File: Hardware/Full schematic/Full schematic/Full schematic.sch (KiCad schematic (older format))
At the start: 170 parts, among them J1 Conn_01x04_Male, J2 Conn_01x03_Male, J3 Conn_01x02_Male, J4 Conn_01x04_Male, J5 Conn_01x03_Male, J6 Conn_01x02_Male, J7 Conn_01x02_Male, J8 Conn_01x02_Male, J9 Conn_01x07_Male, K1 EDR101A0500, K2 EDR101A0500, K3 EDR101A0500, K4 EDR101A0500, K5 EDR101A0500, K6 EDR101A0500, Q1 BC847, Q10 IRLML2502, Q11 IRLML2502, Q12 IRLML2502, Q13 IRLML2502, Q2 BSS138, Q3 BC847, Q4 IRF610, Q5 BSS138, Q6 BFS17, Q7 AFT05MS003N, Q8 IRLML2502, Q9 IRLML2502, U1 74LVC2T45DC, U2 74LVC2T45DC, U3 AD9835, U4 ICS501, X1 50MHz

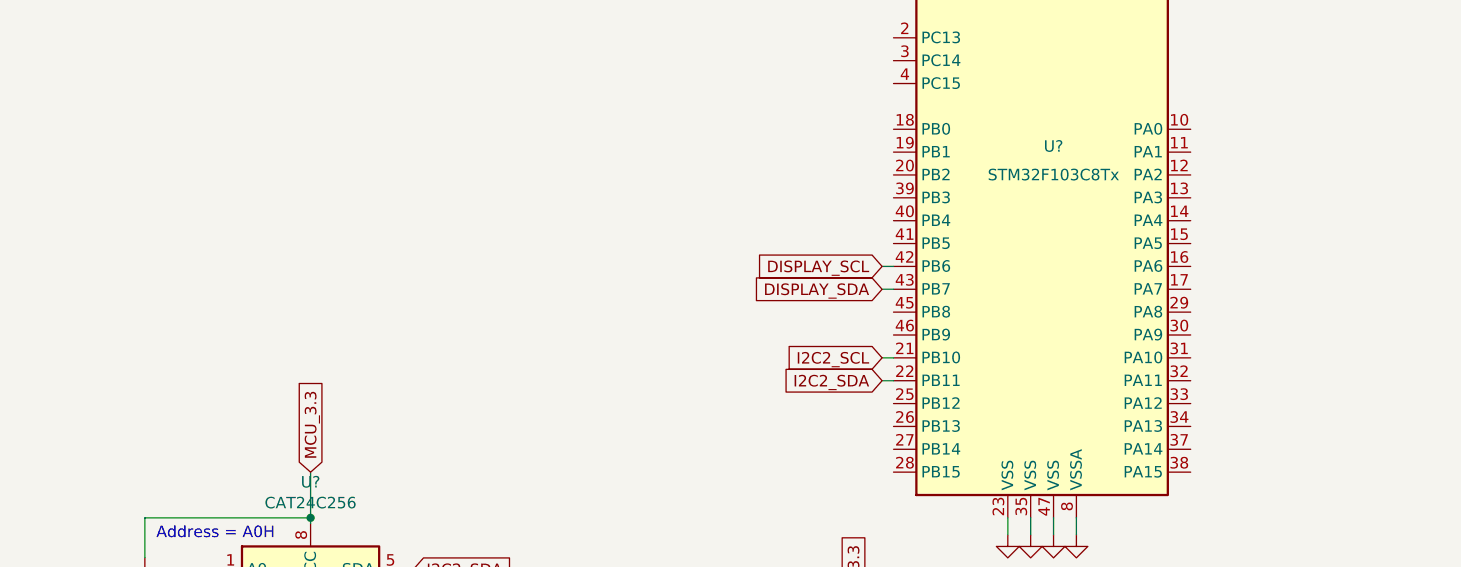
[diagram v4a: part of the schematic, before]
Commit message: Able to get packets via bluetooth
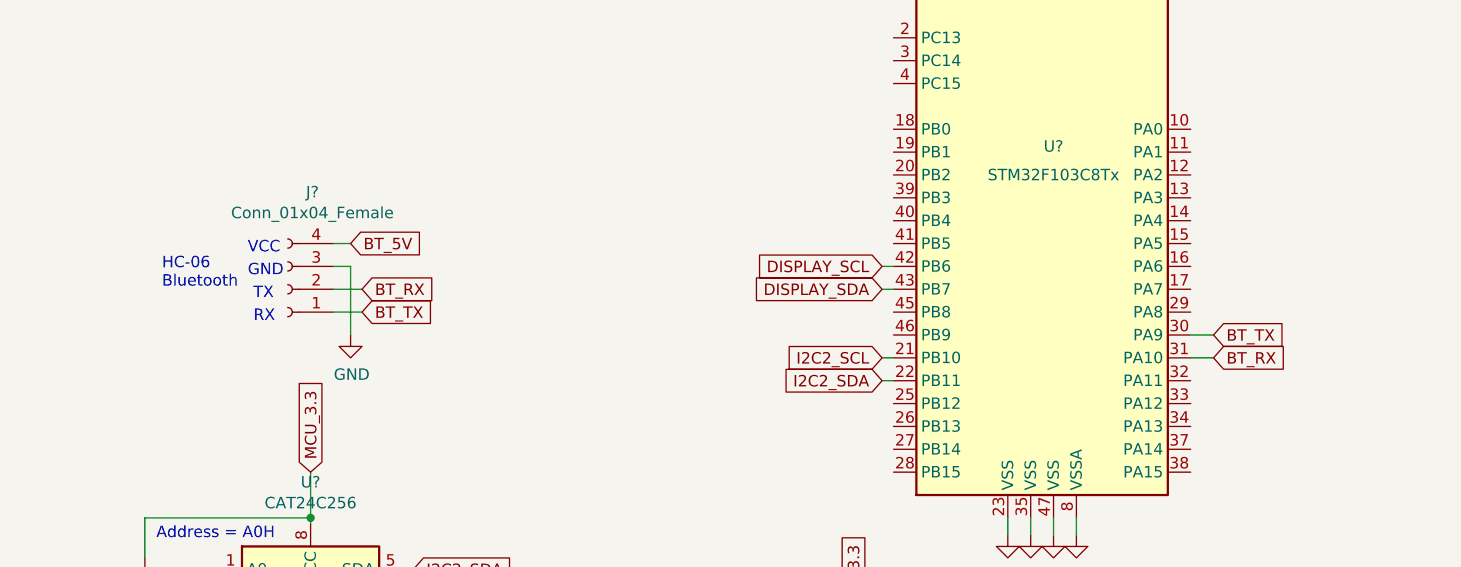
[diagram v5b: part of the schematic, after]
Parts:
- added J?: Conn_01x04_Female, symbol Connector:Conn_01x04_Female
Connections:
- net GND: now also J?.3 (Pin_3)
- net BT_TX: now reaches U?.30 (PA9)
- net BT_TX: now also J?.1 (Pin_1)
- net BT_RX: now reaches U?.31 (PA10)
- net BT_RX: now also J?.2 (Pin_2)
- new net BT_5V: J?.4 (Pin_4)
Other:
- note added: "HC-06\nBluetooth"
- note added: "RX"
- note added: "TX"
- note added: "VCC"
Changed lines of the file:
@@
 Text Notes 5725 16075 0    50   ~ 0
 Address = A0H
+$Comp
+L Connector:Conn_01x04_Female J?
+U 1 1 608B1D74
+P 6300 14975
+F 0 "J?" H 6192 14550 50  0000 C CNN
+F 1 "Conn_01x04_Female" H 6192 14641 50  0000 C CNN
+F 2 "" H 6300 14975 50  0001 C CNN
+F 3 "~" H 6300 14975 50  0001 C CNN
+	1    6300 14975
+	-1   0    0    1
+$EndComp
+Text Notes 6150 15125 0    50   ~ 0
+RX
+Text Notes 6150 15025 0    50   ~ 0
+TX
+Text Notes 6125 14925 0    50   ~ 0
+GND
+Text Notes 6125 14825 0    50   ~ 0
+VCC
+Text Notes 5750 14975 0    50   ~ 0
+HC-06\nBluetooth
+$Comp
+L power:GND #PWR?
+U 1 1 6097477B
+P 6575 15175
+F 0 "#PWR?" H 6575 14925 50  0001 C CNN
+F 1 "GND" H 6580 15002 50  0000 C CNN
+F 2 "" H 6575 15175 50  0001 C CNN
+F 3 "" H 6575 15175 50  0001 C CNN
+	1    6575 15175
+	1    0    0    -1
+$EndComp
+Wire Wire Line
+	6575 15175 6575 14875
+Wire Wire Line
+	6575 14875 6500 14875
+Text GLabel 6575 14775 2    50   Input ~ 0
+BT_5V
+Wire Wire Line
+	6575 14775 6500 14775
+Text GLabel 10350 15175 2    50   Input ~ 0
+BT_TX
+Text GLabel 10350 15275 2    50   Input ~ 0
+BT_RX
+Wire Wire Line
+	10350 15175 10250 15175
+Wire Wire Line
+	10350 15275 10250 15275
+Text GLabel 6625 15075 2    50   Input ~ 0
+BT_TX
+Text GLabel 6625 14975 2    50   Input ~ 0
+BT_RX
+Wire Wire Line
+	6500 14975 6625 14975
+Wire Wire Line
+	6500 15075 6625 15075
 $EndSCHEMATC

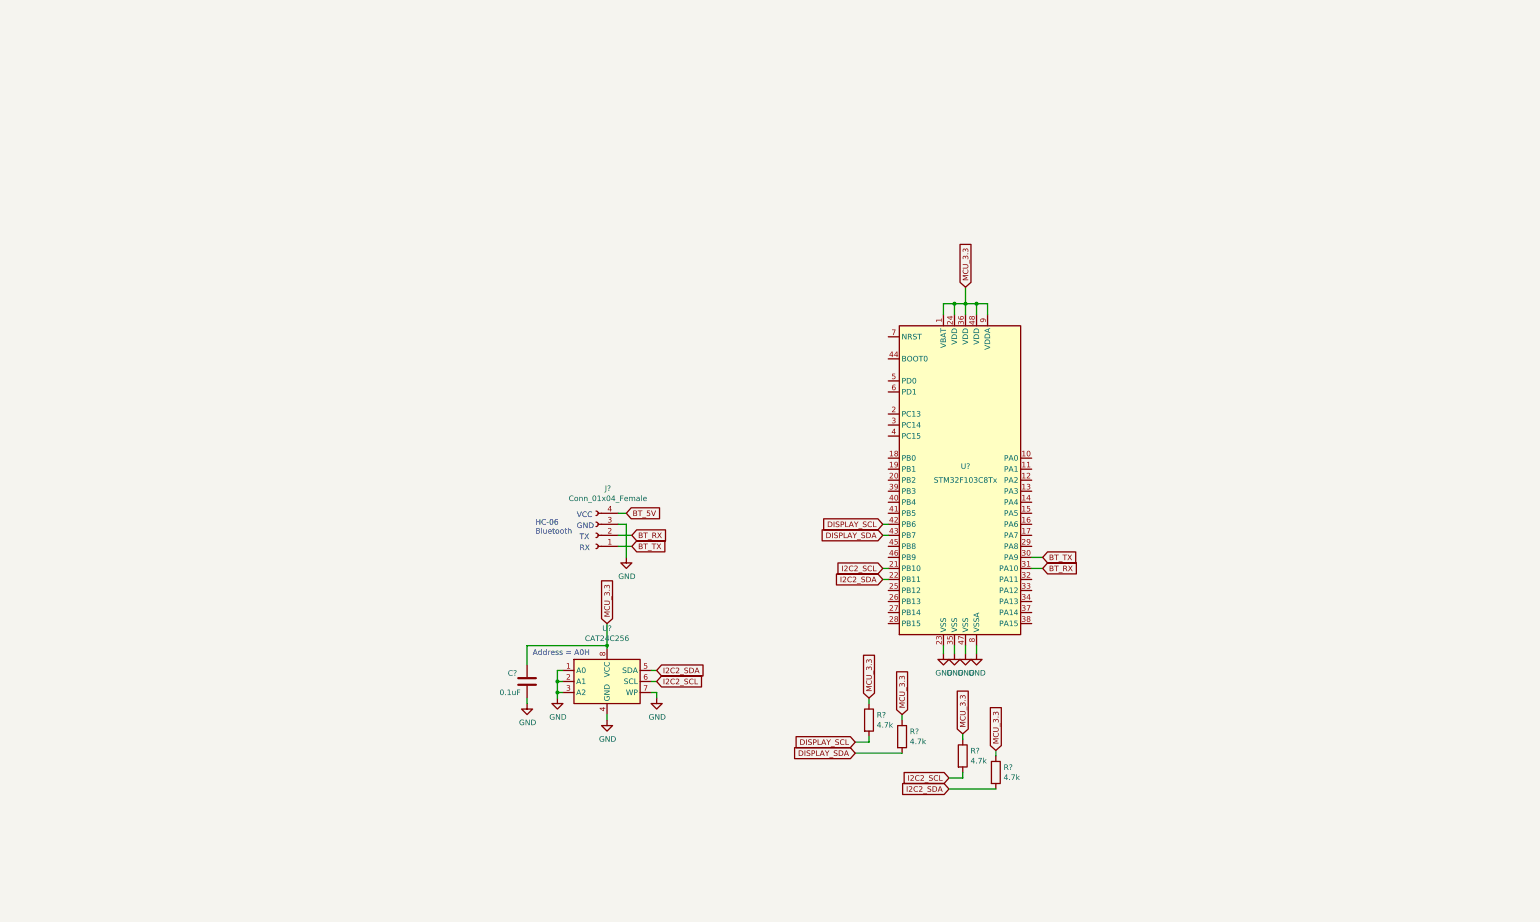
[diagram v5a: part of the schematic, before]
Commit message: Added some voltage regulators
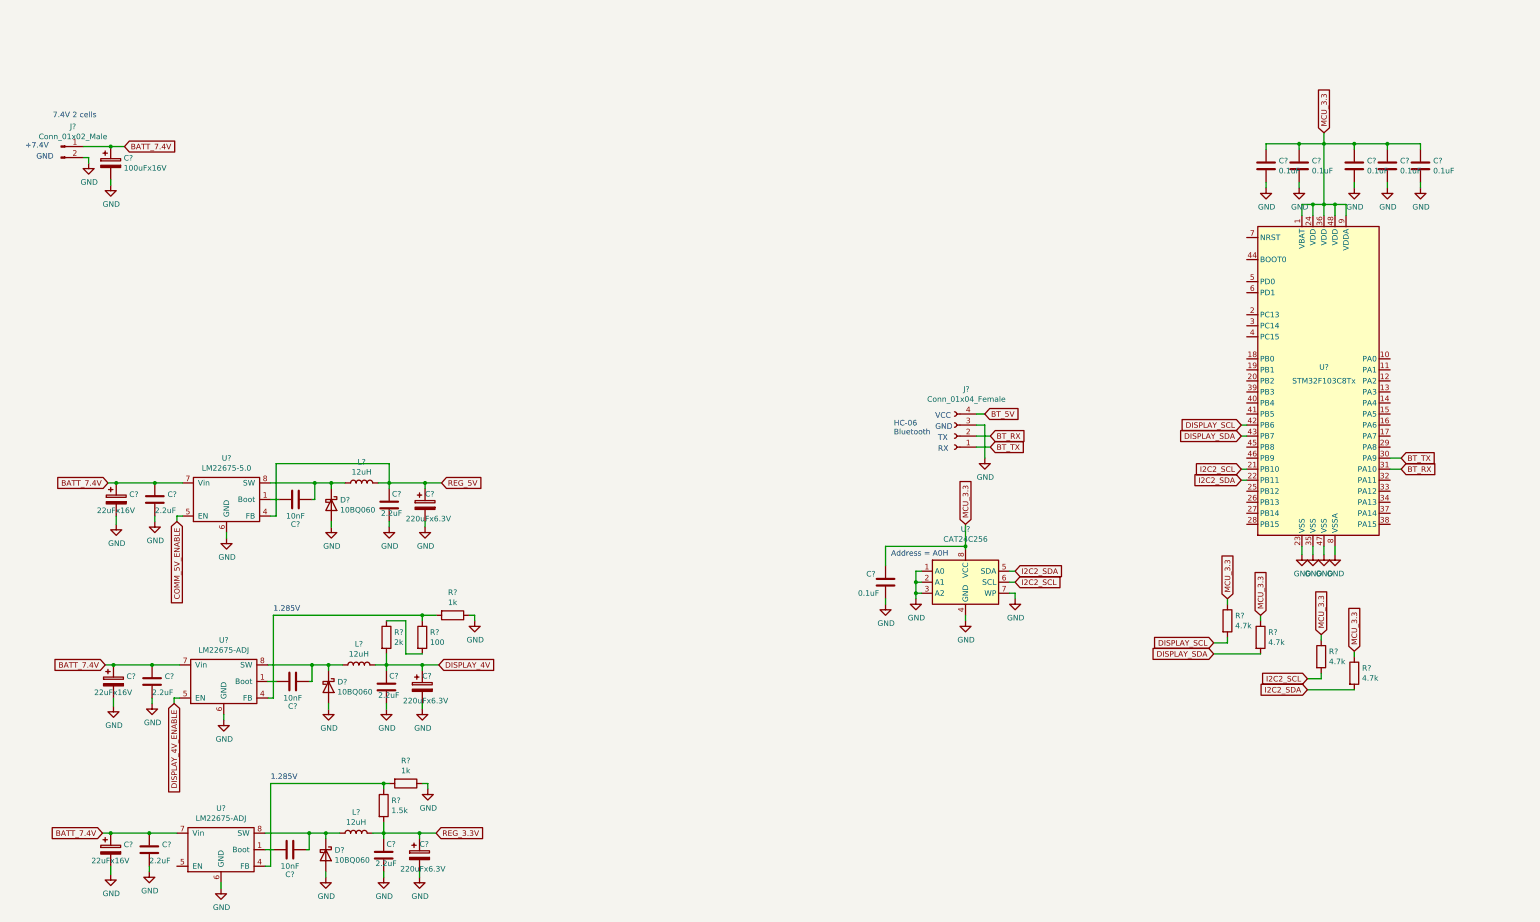
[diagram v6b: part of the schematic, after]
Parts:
- added C? (x5): 0.1uF, symbol Device:C
- added C?: 100uFx16V, symbol Device:CP
- added C? (x6): 2.2uF, symbol Device:C
- added C? (x3): 22uFx16V, symbol Device:CP
- added C? (x3): 10nF, symbol Device:C
- added C? (x3): 220uFx6.3V, symbol Device:CP
- added D? (x3): 10BQ060, symbol Device:D_Schottky
- added J?: Conn_01x02_Male, symbol Connector:Conn_01x02_Male
- added L? (x3): 12uH, symbol Device:L
- added R?: 2k, symbol Device:R
- added R? (x2): 1k, symbol Device:R
- added R?: 100, symbol Device:R
- added R?: 1.5k, symbol Device:R
- added U?: LM22675-5.0, symbol Fossa_library:LM22675-5.0
- added U? (x2): LM22675-ADJ, symbol Fossa_library:LM22675-5.0
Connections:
- net GND: now also C?.2, C?.2, C?.2, C?.2, C?.2, C?.2, C?.2, C?.2, C?.2, C?.2, C?.2, C?.2, C?.2, C?.2, C?.2, C?.2, C?.2, C?.2, D?.2 (A), D?.2 (A), D?.2 (A), J?.2 (Pin_2), R?.1, R?.1, U?.6 (GND), U?.6 (GND), U?.6 (GND)
- net MCU_3.3: now also C?.1, C?.1, C?.1, C?.1, C?.1
- new net: C?.2, U?.1 (Boot) (x3)
- new net: C?.1, D?.1 (K), L?.1, U?.8 (SW) (x3)
- new net: R?.1, R?.2, U?.4 (FB) (x2)
- new net: R?.1, R?.2
- new net BATT_7.4V: C?.1, C?.1, C?.1, C?.1, C?.1, C?.1, C?.1, J?.1 (Pin_1), U?.7 (Vin), U?.7 (Vin), U?.7 (Vin)
- new net COMM_5V_ENABLE: U?.5 (EN)
- new net DISPLAY_4V: C?.1, C?.1, L?.2, R?.2
- new net DISPLAY_4V_ENABLE: U?.5 (EN)
- new net REG_3.3V: C?.1, C?.1, L?.2, R?.2
- new net REG_5V: C?.1, C?.1, L?.2, U?.4 (FB)
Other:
- note added: "+7.4V"
- note added: "1.285V"
- note added: "7.4V 2 cells"
- moved on the sheet: C?, J?, R?, U?

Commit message: Switching regulators to feed my fox
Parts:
- removed C25: 1000uF x 25V, Capacitor_THT:CP_Radial_D10.0mm_P5.00mm, symbol Device:CP
- removed C? (x6): 2.2uF, symbol Device:C
- removed C? (x3): 22uFx16V, symbol Device:CP
- removed C? (x3): 10nF, symbol Device:C
- removed C? (x3): 220uFx6.3V, symbol Device:CP
- removed D? (x3): 10BQ060, symbol Device:D_Schottky
- removed L? (x3): 12uH, symbol Device:L
- removed R?: 2k, symbol Device:R
- removed R? (x2): 1k, symbol Device:R
- removed R?: 100, symbol Device:R
- removed R?: 1.5k, symbol Device:R
- removed U?: LM22675-5.0, symbol Fossa_library:LM22675-5.0
- removed U? (x2): LM22675-ADJ, symbol Fossa_library:LM22675-5.0
- added C? (x5): 22uFx16V, symbol Device:CP
- added C? (x10): 4.7uF, symbol Device:C
- added C? (x2): 2.2uF, symbol Device:C
- added C?: 2.7nF, symbol Device:C
- added C? (x3): 10nF, symbol Device:C
- added C?: 220uFx25V, symbol Device:CP
- added C?: 180pF, symbol Device:C
- added C?: 0.1uF, symbol Device:C
- added C?: 220uFx16V, symbol Device:CP
- added C? (x3): 1nF, symbol Device:C
- added C? (x3): 220uFx6.3V, symbol Device:CP
- added D?: 1N5819, symbol Device:D_Schottky
- added D? (x4): MBR0520, symbol Device:D_Schottky
- added D? (x3): 1N4148, Diode_THT:D_DO-35_SOD27_P7.62mm_Horizontal, symbol Diode:1N4148
- added L? (x5): 10uH, symbol Device:L
- added R?: 100k, symbol Device:R
- added R?: 120k, symbol Device:R
- added R?: 13k, symbol Device:R
- added R?: 51k, symbol Device:R
- added R? (x3): 10k, symbol Device:R
- added R?: 6.2k, symbol Device:R
- added R?: 39k, symbol Device:R
- added R?: 30k, symbol Device:R
- added U?: LM27313XMF, Package_TO_SOT_SMD:SOT-23-5, symbol Regulator_Switching:LM27313XMF
- added U? (x3): LM2734X, Package_TO_SOT_SMD:TSOT-23-6, symbol Regulator_Switching:LM2734X
- added U?: AD5245BRJZ10, symbol Fossa_library:AD5245
- added U?: LM2731YMF, Package_TO_SOT_SMD:SOT-23-5, symbol Regulator_Switching:LM2731YMF
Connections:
- net BATT_7.4V: now also C?.1, C?.1, C?.1, C?.1, C?.1, C?.1, C?.1, C?.1, C?.1, C?.1, L?.1, L?.1, U?.4 (EN), U?.5 (VIN), U?.5 (VIN), U?.5 (VIN), U?.5 (VIN), U?.5 (VIN)
- net COMM_5V_ENABLE: now also U?.4 (EN)
- net DISPLAY_4V: now also C?.1, C?.1, C?.1, D?.2 (A), L?.2, R?.1
- net DISPLAY_4V_ENABLE: now also U?.4 (EN)
- net GND: now also C?.2, C?.2, C?.2, C?.2, C?.2, C?.2, C?.2, C?.2, C?.2, C?.2, C?.2, C?.2, C?.2, C?.2, C?.2, C?.2, C?.2, C?.2, C?.2, C?.2, C?.2, C?.2, C?.2, D?.2 (A), D?.2 (A), D?.2 (A), R?.2, R?.2, R?.2, R?.2, U?.2 (GND), U?.2 (GND), U?.2 (GND), U?.2 (GND), U?.2 (GND), U?.3 (GND), U?.6 (AD0), U?.7 (B)
- net I2C2_SCL: now also U?.4 (SCL)
- net I2C2_SDA: now also U?.5 (SDA)
- net MCU_3.3: now also C?.1, U?.2 (Vdd)
- net PWR_3.5_OUT: now also C?.1, C?.1, C?.1, C?.1, C?.1, D?.1 (K), R?.1; no longer J4.4 (Pin_4)
- net REG_3.3V: now also C?.1, C?.1, C?.1, D?.2 (A), L?.2, R?.1
- net REG_5V: now also C?.1, C?.1, C?.1, D?.2 (A), L?.2, R?.1
- new net: D?.2 (A), L?.2, U?.1 (SW) (x2)
- new net: C?.2, R?.1, R?.2, U?.3 (FB) (x5)
- new net: C?.2, D?.1 (K), U?.1 (BOOST) (x3)
- new net: C?.1, D?.1 (K), L?.1, U?.6 (SW) (x3)
- new net: R?.2, U?.1 (W), U?.8 (A)
- new net ENABLE_12V: U?.4 (EN)
- new net ENABLE_3.5_VOUT: U?.4 (EN)
- new net REG_12V: C?.1, C?.1, C?.1, D?.1 (K), R?.1
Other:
- note added: "1 - Enable\n0 - Disable"
- note added: "8-20V"
- note removed: "1.285V"
- moved on the sheet: C?, J?
